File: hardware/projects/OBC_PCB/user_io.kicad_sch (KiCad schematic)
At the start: 24 parts, among them J5 TC2030-CTX-NL, SW1 PREV, SW2 NEXT, SW3 SELECT / POWER, SW4 BACK, U10 SN74LVC2G00DCTR

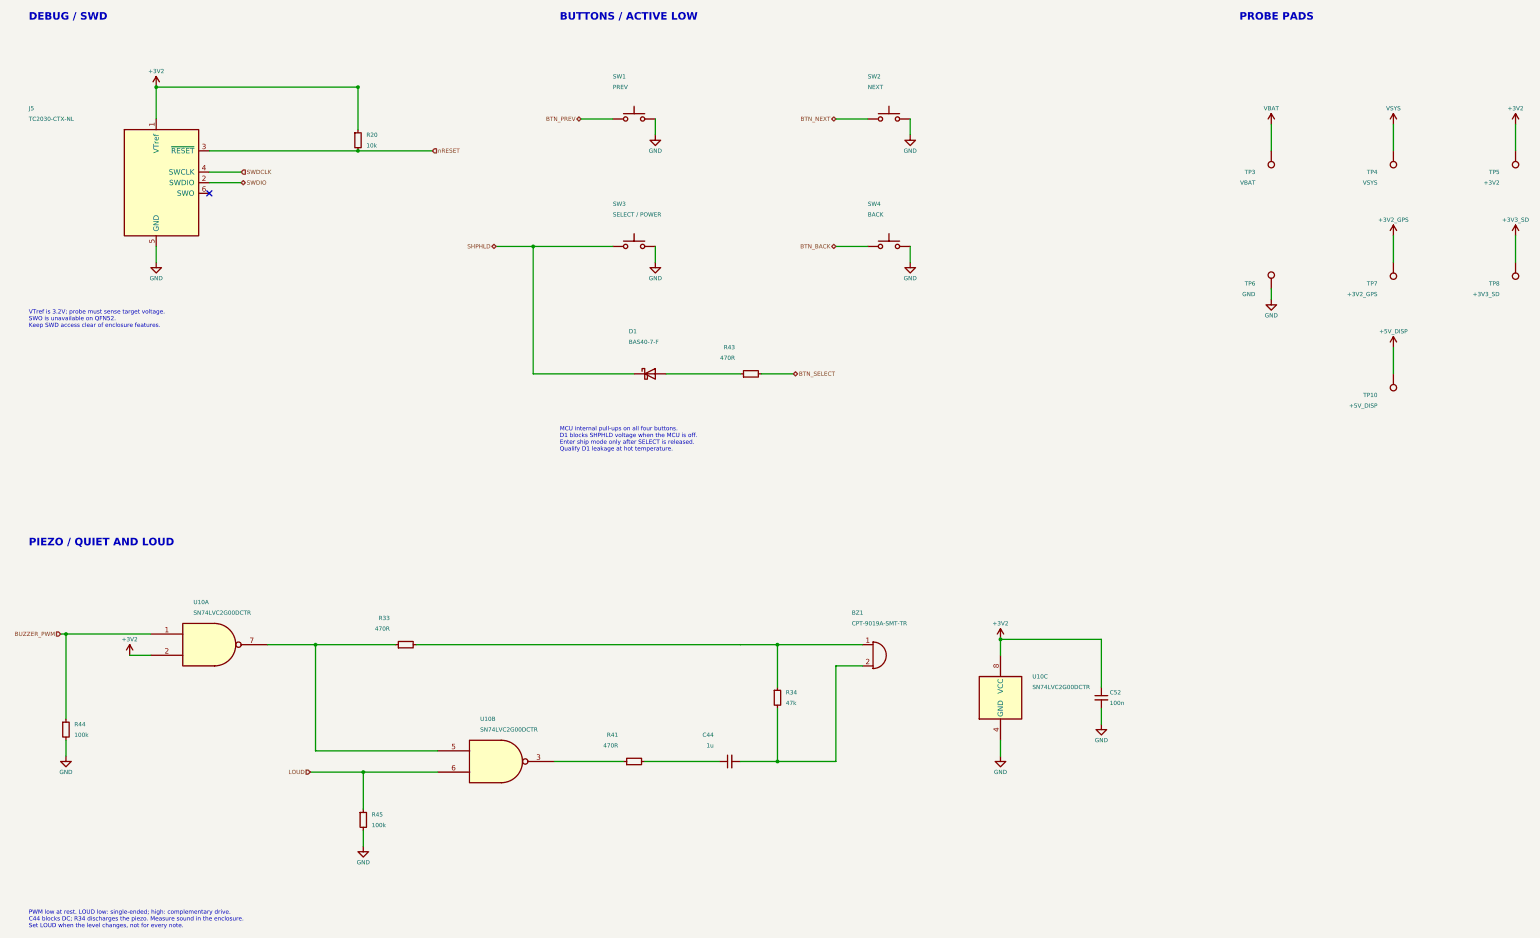
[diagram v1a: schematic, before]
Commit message: hardware: save current KiCad schematic and project files
Retain the saved KiCad 10 schematic files and project sheet list.
The native netlist matches the committed placement circuit: 172
components and 140 nets. Public docs unchanged.
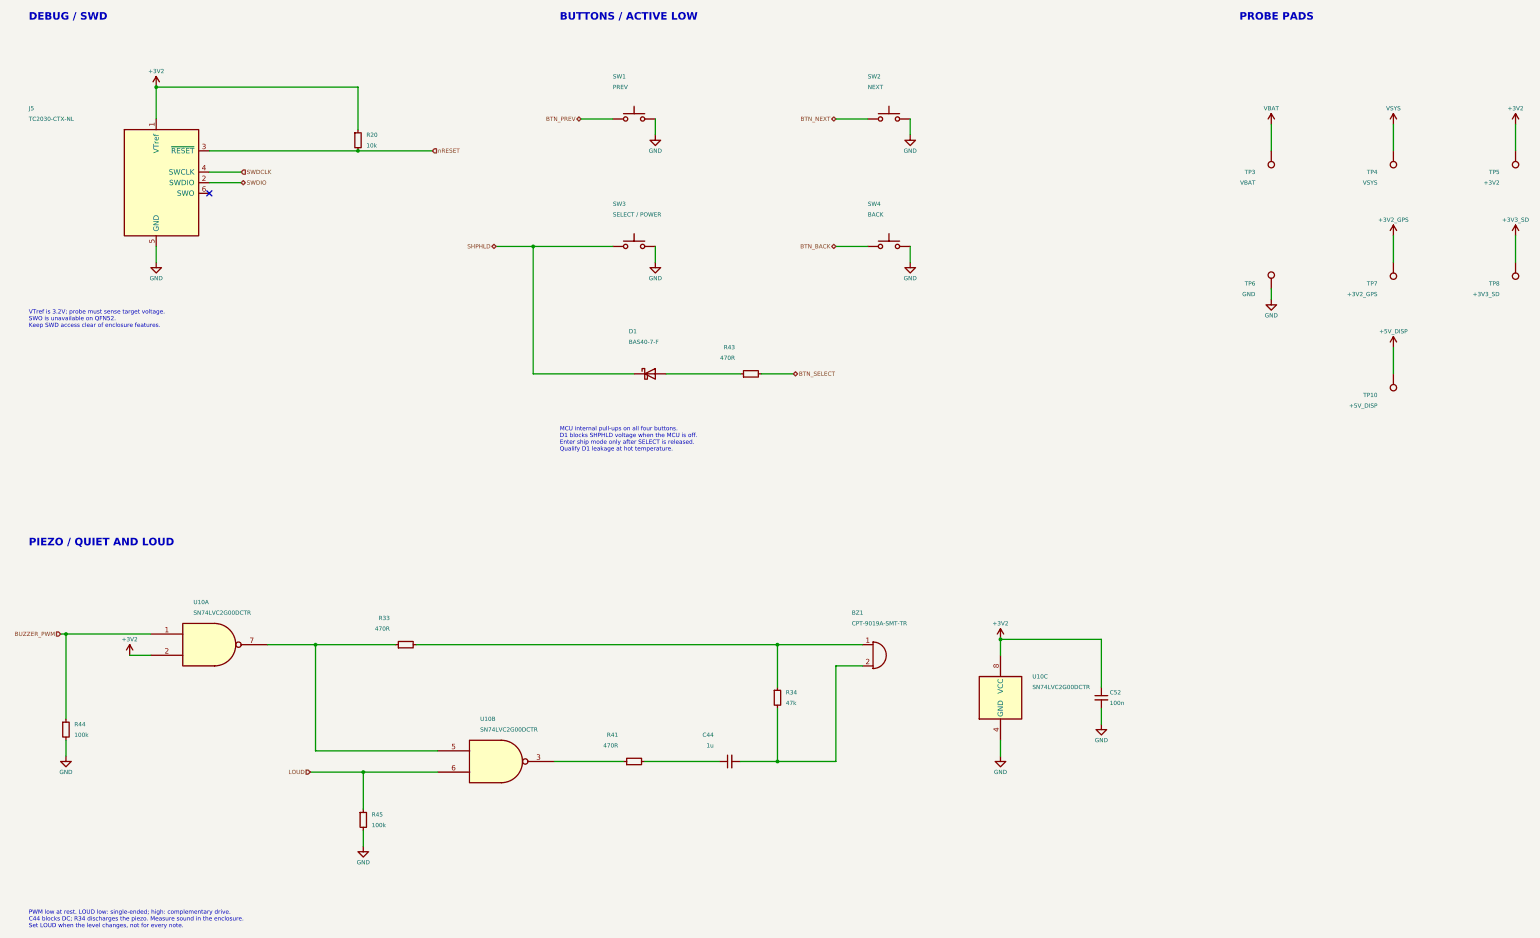
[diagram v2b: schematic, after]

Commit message: hardware: add editable KiCad BOM and schematic exports
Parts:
- BZ1: Mouser (none) -> https://eu.mouser.com/en/ProductDetail/Same-Sky/CPT-9019A-S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; Price breaks EUR (none) -> 1:1.08;10:0.815;25:0.734;50:0.679;100:0.63;250:0.576;500:0.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; Price checked (none) -> 2026-10-02; Price source (none) -> https://eu.mouser.com/en/ProductDetail/Same-Sky/CPT-9019A-S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; Sourcing notes (none) -> Backorder shown; confirm delivery.
- C44: DigiKey (none) -> https://www.digikey.jp/ja/products/detail/yageo/CC0603KRX7R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; MPN (none) -> CC0603KRX7R8BB105; Manufacturer (none) -> YAGEO; Mouser (none) -> https://www.mouser.de/de/ProductDetail/YAGEO/CC0603KRX7R8BB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; Price breaks EUR (none) -> 1:0.215;10:0.108;100:0.08;500:0.065;1000:0.054; Price checked (none) -> 2026-10-02; Price source (none) -> https://www.mouser.de/de/ProductDetail/YAGEO/CC0603KRX7R8BB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; Selection notes (none) -> Candidate; verify DC-bias, temperature and tolerance agains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
- C52: DigiKey (none) -> https://www.digikey.de/en/products/detail/murata-electronic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; MPN (none) -> GRM155R71A104KA01D; Manufacturer (none) -> Murata; Price breaks EUR (none) -> 1:0.09000;10:0.02100;50:0.01400;100:0.01190;500:0.00830; Price checked (none) -> 2026-10-02; Price source (none) -> https://www.digikey.de/en/products/detail/murata-electronic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
- D1: Mouser (none) -> https://www.mouser.it/ProductDetail/Diodes-Incorporated/BAS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; Price breaks EUR (none) -> 1:0.249;10:0.163;100:0.102;500:0.079;1000:0.069; Price checked (none) -> 2026-10-02; Price source (none) -> https://www.mouser.it/ProductDetail/Diodes-Incorporated/BAS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
- R20: MPN (none) -> RC0402FR-0710KL; Manufacturer (none) -> YAGEO; Mouser (none) -> https://www.mouser.de/en/ProductDetail/YAGEO/RC0402FR-0710K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; Power 63mW -> 62.5mW; Price breaks EUR (none) -> 1:0.086;10:0.009;100:0.006;1000:0.005;2500:0.003; Price checked (none) -> 2026-10-02; Price source (none) -> https://www.mouser.de/en/ProductDetail/YAGEO/RC0402FR-0710K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
- R33, R41: MPN (none) -> RC0402FR-07470RL; Manufacturer (none) -> YAGEO; Mouser (none) -> https://eu.mouser.com/en/ProductDetail/YAGEO/RC0402FR-07470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; Power 63mW -> 62.5mW; Price breaks EUR (none) -> 1:0.086;10:0.009;100:0.006;1000:0.005;2500:0.003; Price checked (none) -> 2026-10-02; Price source (none) -> https://eu.mouser.com/en/ProductDetail/YAGEO/RC0402FR-07470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
- R34: MPN (none) -> RC0402FR-0747KL; Manufacturer (none) -> YAGEO; Mouser (none) -> https://eu.mouser.com/en/ProductDetail/YAGEO/RC0402FR-0747K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; Power (none) -> 62.5mW; Price breaks EUR (none) -> 1:0.086;10:0.009;100:0.006;1000:0.005;2500:0.003; Price checked (none) -> 2026-10-02; Price source (none) -> https://eu.mouser.com/en/ProductDetail/YAGEO/RC0402FR-0747K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; Technology (none) -> Thick film; Voltage (none) -> 50V
- R43: MPN (none) -> RC0402FR-07470RL; Manufacturer (none) -> YAGEO; Mouser (none) -> https://eu.mouser.com/en/ProductDetail/YAGEO/RC0402FR-07470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; Power (none) -> 62.5mW; Price breaks EUR (none) -> 1:0.086;10:0.009;100:0.006;1000:0.005;2500:0.003; Price checked (none) -> 2026-10-02; Price source (none) -> https://eu.mouser.com/en/ProductDetail/YAGEO/RC0402FR-07470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; Technology (none) -> Thick film; Voltage (none) -> 50V
- R44, R45: MPN (none) -> RC0402FR-07100KL; Manufacturer (none) -> YAGEO; Mouser (none) -> https://www.mouser.fr/en/ProductDetail/YAGEO/RC0402FR-07100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; Power (none) -> 62.5mW; Price breaks EUR (none) -> 1:0.086;10:0.009;100:0.006;1000:0.005;2500:0.003; Price checked (none) -> 2026-10-02; Price source (none) -> https://www.mouser.fr/en/ProductDetail/YAGEO/RC0402FR-07100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; Technology (none) -> Thick film; Voltage (none) -> 50V
- SW1, SW2, SW3, SW4: Mouser (none) -> https://www.mouser.lu/ProductDetail/E-Switch/TL1016AAF220QG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; Price breaks EUR (none) -> 1:0.318;10:0.278;25:0.257;100:0.23;250:0.213; Price checked (none) -> 2026-10-02; Price source (none) -> https://www.mouser.lu/ProductDetail/E-Switch/TL1016AAF220QG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; Sourcing notes (none) -> Volume price needs refresh; last published cut-tape break u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
- U10: Mouser (none) -> https://www.mouser.es/ProductDetail/Texas-Instruments/SN74L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; Price breaks EUR (none) -> 1:0.697;10:0.501;25:0.451;100:0.396;250:0.369;500:0.353;100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; Price checked (none) -> 2026-10-02; Price source (none) -> https://www.mouser.es/ProductDetail/Texas-Instruments/SN74L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
